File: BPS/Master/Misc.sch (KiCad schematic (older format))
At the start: 27 parts, among them J12 Conn_01x06, J14 Conn_01x06, J15 Conn_01x06, J3 FrontFans, J4 BackFans, Q6 DMP3013SFV

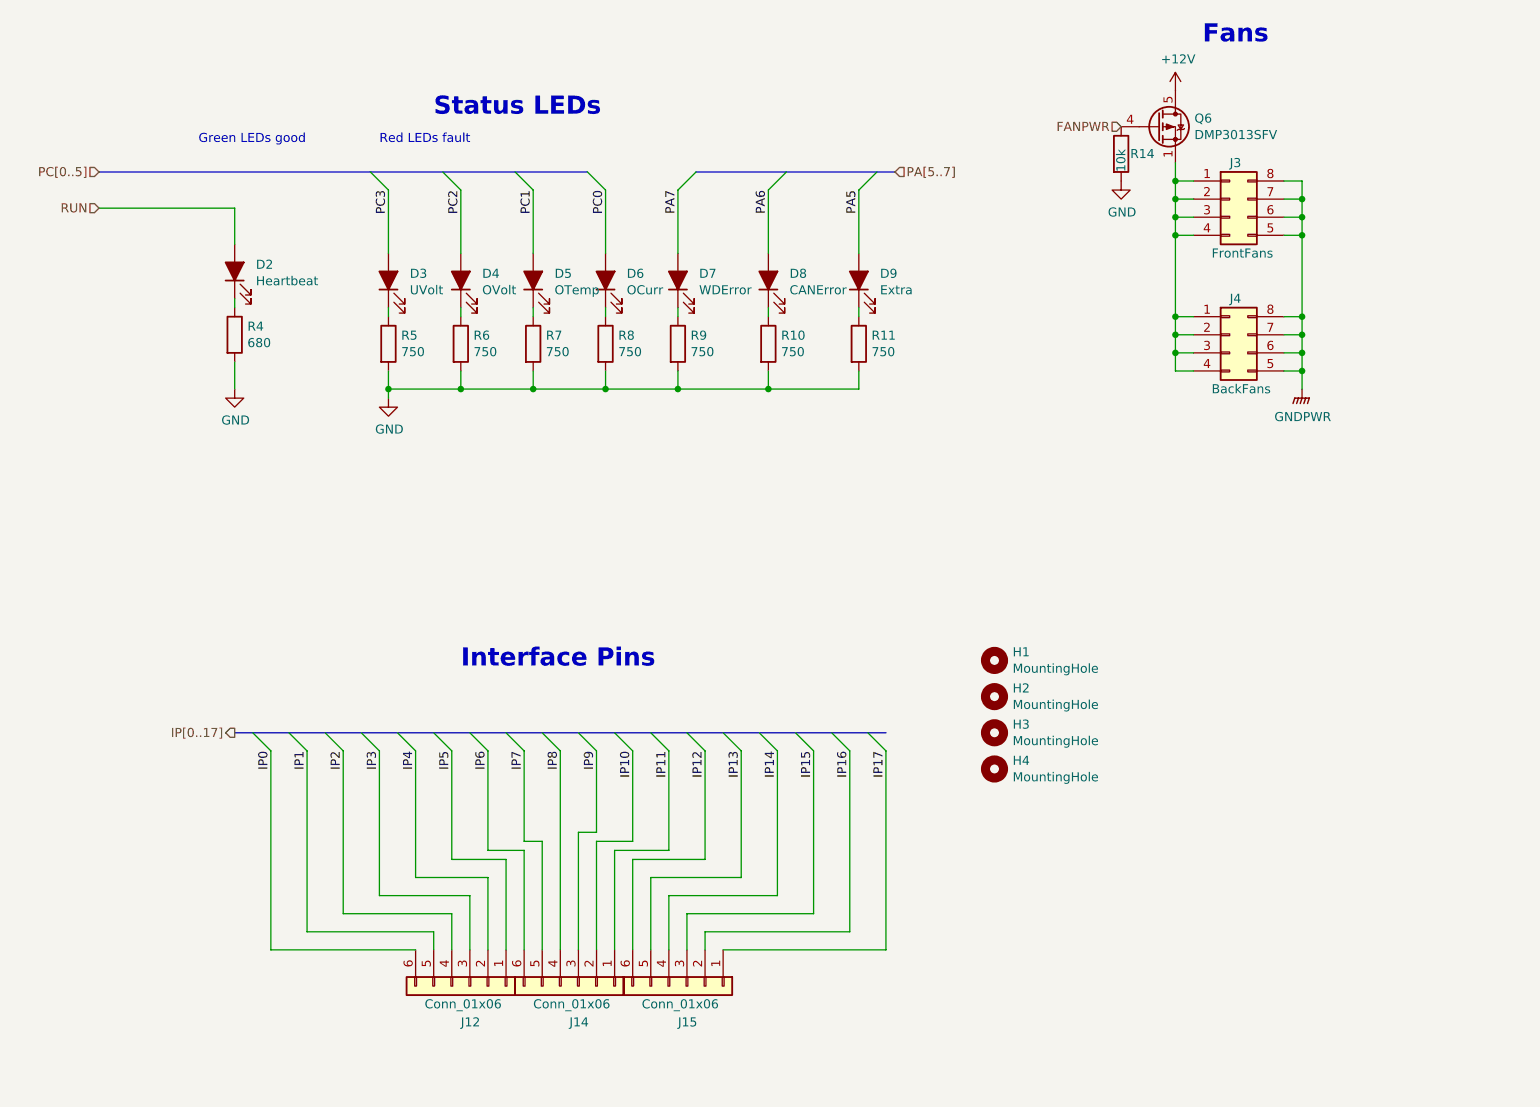
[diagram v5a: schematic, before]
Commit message: Reverts edited files that are not related to the FanBoard back to master branch's versions
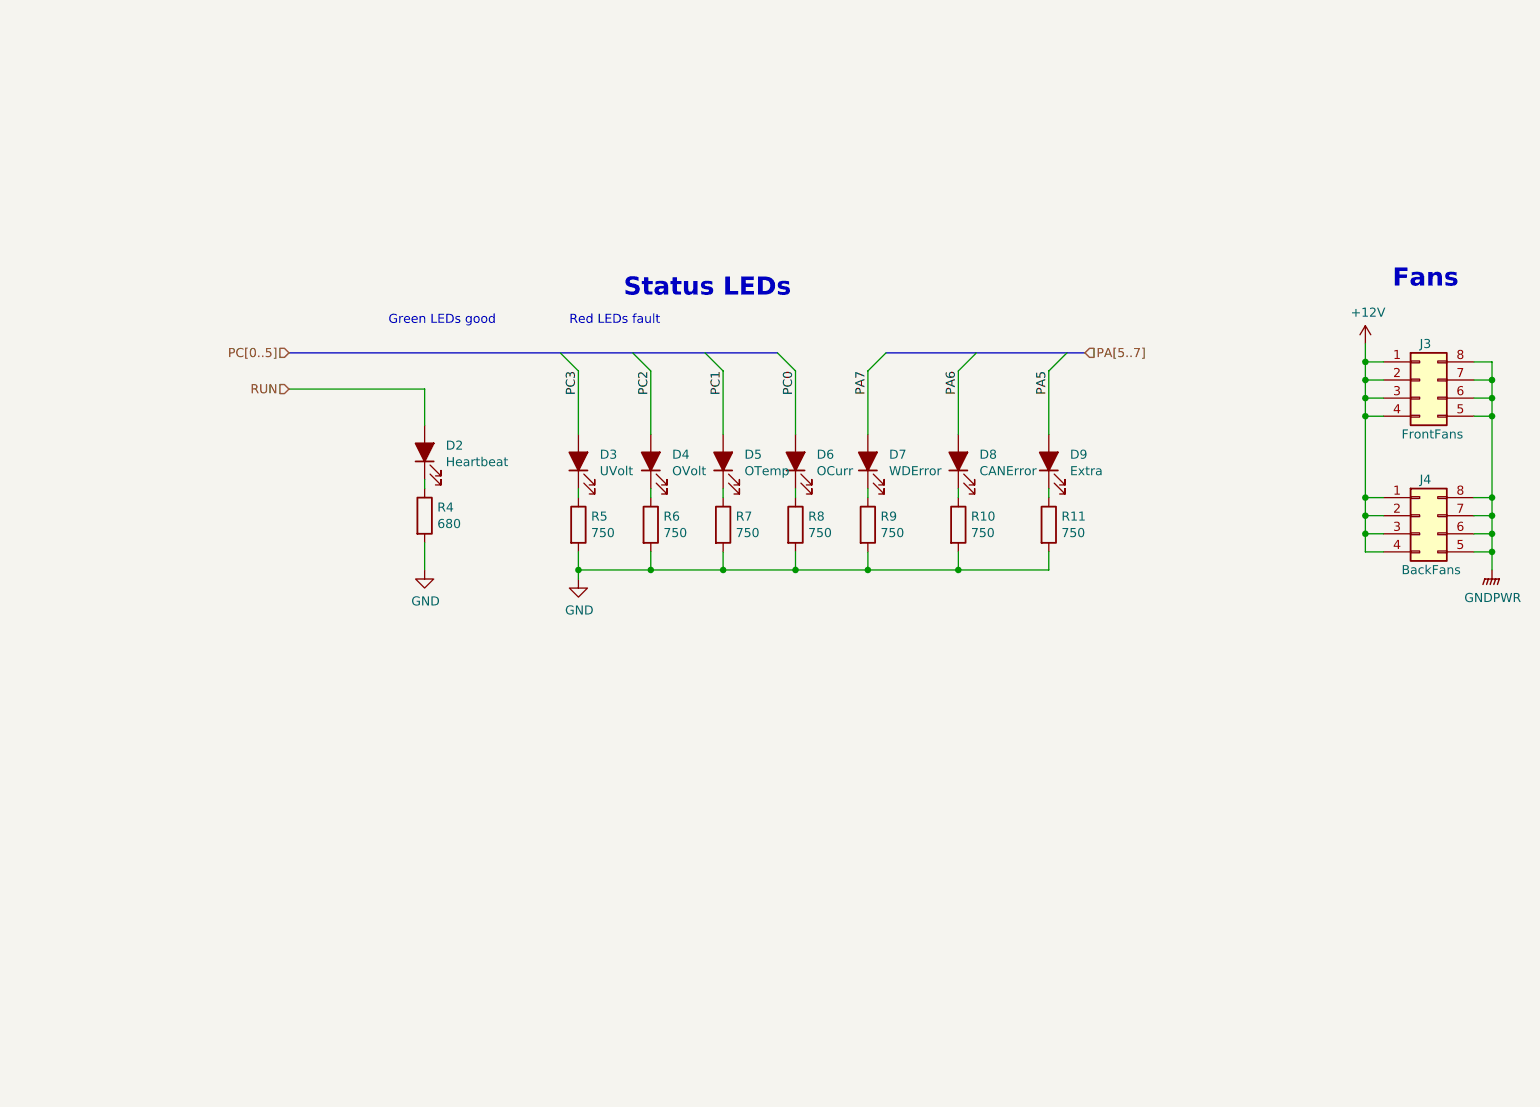
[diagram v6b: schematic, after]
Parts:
- removed H1, H2, H3, H4: MountingHole, MountingHole:MountingHole_2.1mm, symbol Mechanical:MountingHole
- removed J12, J14, J15: Conn_01x06, Connector_PinHeader_2.54mm:PinHeader_1x06_P2.54mm_Vertical, symbol Connector_Generic:Conn_01x06
- removed Q6: DMP3013SFV, Package_SON:Diodes_PowerDI3333-8, symbol Transistor_FET:DMP3013SFV
- removed R14: 10k, Resistor_SMD:R_0805_2012Metric, symbol Device:R
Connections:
- net +12V: now also J3.1 (Pin_1), J3.2 (Pin_2), J3.3 (Pin_3), J3.4 (Pin_4), J4.1 (Pin_1), J4.2 (Pin_2), J4.3 (Pin_3), J4.4 (Pin_4)
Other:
- note removed: "Interface Pins"
- moved on the sheet: D2, D3, D4, D5, D6, D7, D8, D9, J3, J4, R10, R11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

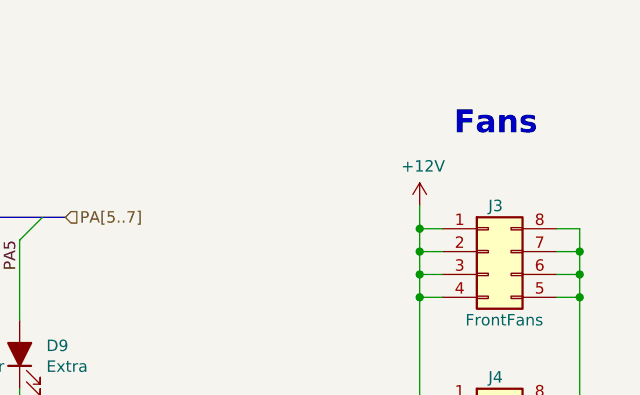
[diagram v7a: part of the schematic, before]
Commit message: Added PWM for fan control. Since max output of pins are 3V, used buttons to connect 12V to fan. Used pin 28 of STM for PWM using Low Power Timer 1.
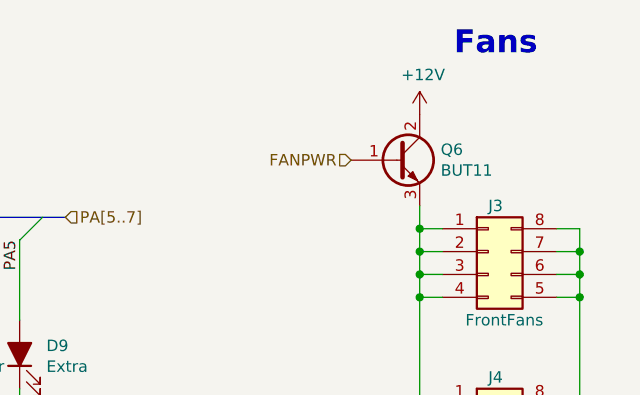
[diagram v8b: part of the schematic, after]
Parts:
- added Q6: BUT11, Package_TO_SOT_THT:TO-220-3_Vertical, symbol Transistor_BJT:BUT11
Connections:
- net +12V: now also Q6.2 (C); no longer J3.1 (Pin_1), J3.2 (Pin_2), J3.3 (Pin_3), J3.4 (Pin_4), J4.1 (Pin_1), J4.2 (Pin_2), J4.3 (Pin_3), J4.4 (Pin_4)
- new net: J3.1 (Pin_1), J3.2 (Pin_2), J3.3 (Pin_3), J3.4 (Pin_4), J4.1 (Pin_1), J4.2 (Pin_2), J4.3 (Pin_3), J4.4 (Pin_4), Q6.3 (E)
- new net FANPWR: Q6.1 (B)
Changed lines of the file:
@@
 	1    0    0    -1
 $EndComp
-Text Notes 8200 2150 0    100  ~ 20
+Text Notes 8200 1800 0    100  ~ 20
 Fans
 $Comp
@@
 F 3 "~" H 8350 3400 50  0001 C CNN
 	1    8350 3400
-	1    0    0    -1
-$EndComp
-$Comp
-L power:+12V #PWR028
-U 1 1 5C39E1C8
-P 8050 2450
-F 0 "#PWR028" H 8050 2300 50  0001 C CNN
-F 1 "+12V" H 8065 2623 50  0000 C CNN
-F 2 "" H 8050 2450 50  0001 C CNN
-F 3 "" H 8050 2450 50  0001 C CNN
-	1    8050 2450
 	1    0    0    -1
 $EndComp
@@
 RUN
 Connection ~ 5800 3700
+Text HLabel 7750 2250 0    50   Input ~ 0
+FANPWR
+$Comp
+L power:+12V #PWR0118
+U 1 1 5EE38D3D
+P 8050 2050
+F 0 "#PWR0118" H 8050 1900 50  0001 C CNN
+F 1 "+12V" H 8065 2223 50  0000 C CNN
+F 2 "" H 8050 2050 50  0001 C CNN
+F 3 "" H 8050 2050 50  0001 C CNN
+	1    8050 2050
+	1    0    0    -1
+$EndComp
 Wire Bus Line
 	5400 2500 6500 2500
 Wire Bus Line
 	2100 2500 4800 2500
+$Comp
+L Transistor_BJT:BUT11 Q6
+U 1 1 5EE3EB2A
+P 7950 2250
+F 0 "Q6" H 8142 2296 50  0000 L CNN
+F 1 "BUT11" H 8142 2205 50  0000 L CNN
+F 2 "Package_TO_SOT_THT:TO-220-3_Vertical" H 8150 2175 50  0001 L CIN
+F 3 "http://www.fairchildsemi.com/ds/BU/BUT11.pdf" H 7950 2250 50  0001 L CNN
+	1    7950 2250
+	1    0    0    -1
+$EndComp
 $EndSCHEMATC
